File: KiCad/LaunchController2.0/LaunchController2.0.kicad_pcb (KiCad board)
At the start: 4 copper layers, 150 x 100 mm, 181 parts, among them J1 CONN_ICSP, J10 CONN_PANEL_BAORD_2, J11 CONN_AUDIO, J12 CONN_SPEAKER, J13 CONN_RS485, J2 CONN_USB, J3 USB_C_Receptacle_USB2.0_16P, J4 TO_CONVERTER, J5 FROM_CONVERTER, J6 DC_IN, J7 CONN_STATUS_PANEL, J8 CONN_BOARD_3, J9 CONN_PANEL_BAORD_1, Q1 TJ8S06M3L, Q2 2SC3325-Y, Q3 TJ8S06M3L, SW1 SW_Push, SW10 SW_Push, SW11 SW_Push, SW12 SW_Push, SW13 SW_Push, SW14 SW_Push, SW15 SW_Push, SW16 SW_Push, SW17 SW_Push, SW2 SW_Push, SW3 SW_Push, SW4 SW_Push, SW5 SW_Push, SW6 SW_Push, SW7 SW_Push, SW8 SW_Push, SW9 SW_Push, U1 ATmega2560-16A, U10 ADM2582E, U11 24LC256, U2 FT232RNL, U3 USBLC6-2SC6, U4 TPS2116DRL, U5 NJM7805SDL1, U6 INA219BIDCNT, U7 INA219BIDCNT, U9 DFPlayer, Y1 HUSG-16.000-20

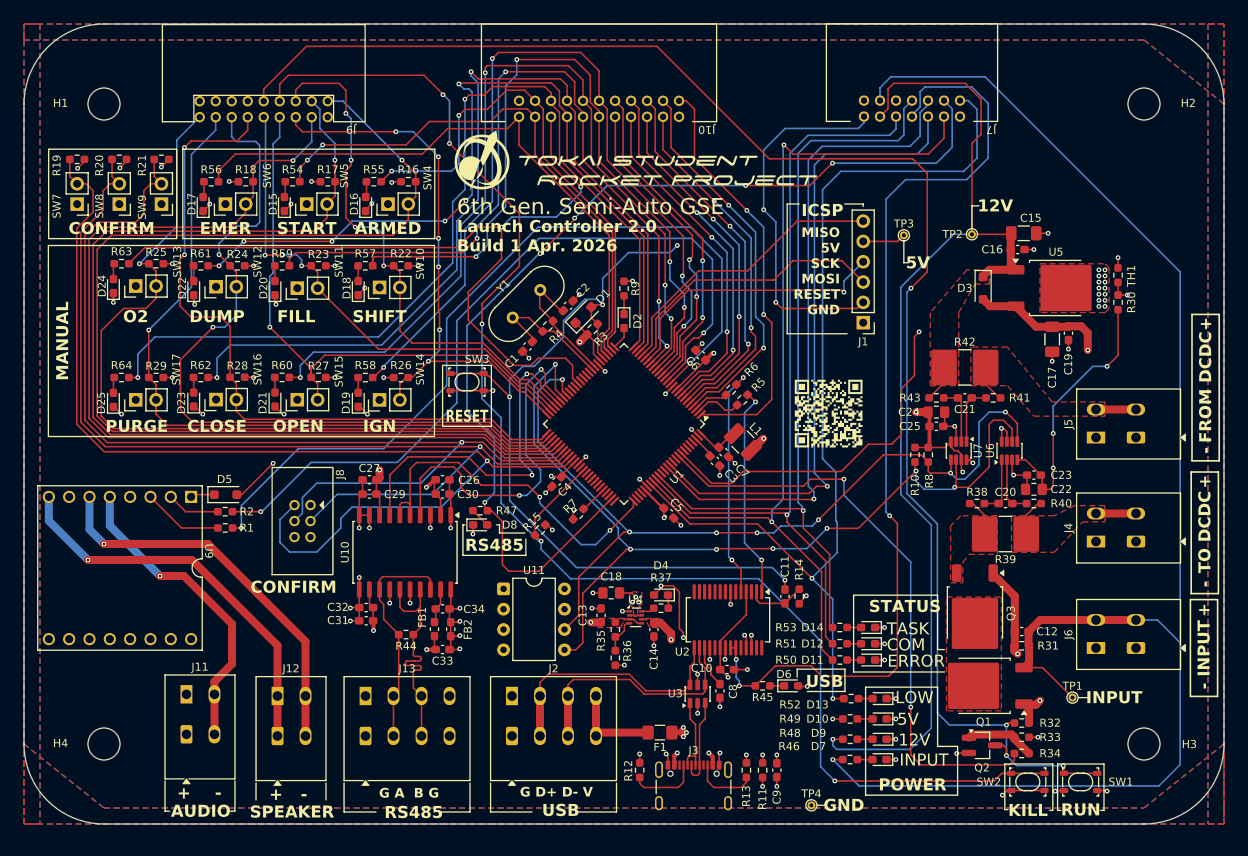
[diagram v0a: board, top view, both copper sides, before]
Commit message: 4層基板から2層基板へ仕様変更
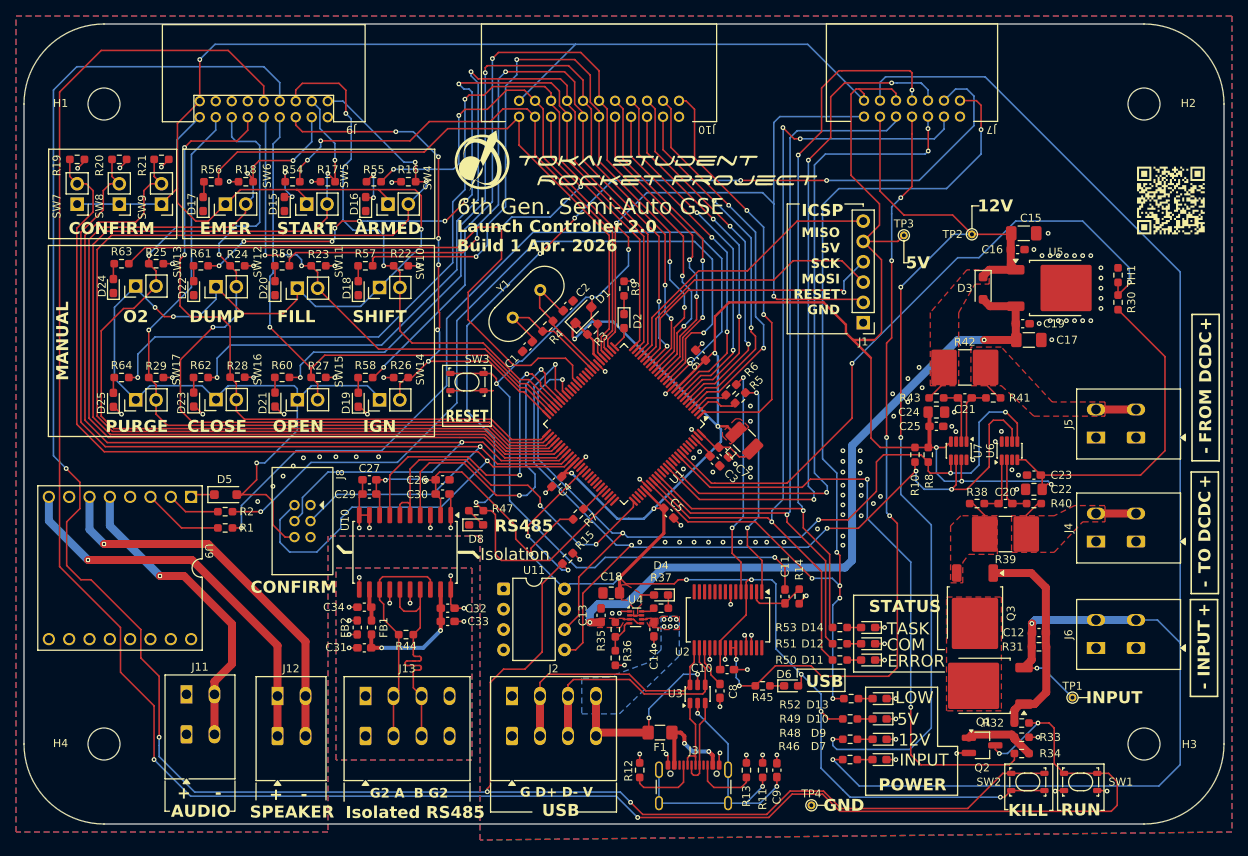
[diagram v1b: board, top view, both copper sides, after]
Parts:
- C33: value 0.01uF -> 0.1uF
- moved G*** 50.4 mm to (219.4, 73.1)
- moved FB2 11.7 mm to (117.7, 126.4)
- moved C32 10.2 mm to (129.0, 124.0), turned to 180 degrees
- moved C34 9.78 mm to (118.5, 123.9), turned to 0 degrees
- moved FB1 7.88 mm to (119.4, 126.4)
- moved C19 5.84 mm to (200.8, 88.5), turned to 180 degrees
- moved R15 4.94 mm to (143.9, 117.8)
- moved C33 3.57 mm to (129.0, 125.7)
- moved C31 3.39 mm to (118.5, 129.0)
- moved C17 2.92 mm to (201.6, 90.5), turned to 180 degrees
- moved R31 2.16 mm to (202.9, 128.9), turned to 0 degrees
- moved C12 2.16 mm to (202.9, 127.1), turned to 0 degrees
- moved D8 0.51 mm to (132.5, 113.6)
- moved R47 0.51 mm to (132.5, 111.8)
- moved R5 0.36 mm to (165.5, 97.7)
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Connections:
- U10 pad 12: /Peripheral/Visoin -> /Peripheral/Visoout
- U10 pad 19: /Peripheral/Visoout -> /Peripheral/Visoin
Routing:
- net CTL_KILL: track 186.2 -> 294.1 mm, vias 5 -> 6
- net CTL_RUN: track 192.7 -> 272.7 mm
- net VIN_5V: track 131.5 -> 89.6 mm
- net GND: track 132.1 -> 92.1 mm, vias 98 -> 144
- net CONN_LED_USB_ACCESS: track 121.4 -> 98.3 mm, vias 3 -> 6
- net CONN_LED_5V: track 699.5 -> 721.8 mm, vias 23 -> 22
- net CONN_LED_12V: track 136.8 -> 126.1 mm, vias 1 -> 3
- net USB_VBUS: track 35.2 -> 24.6 mm, vias 2 -> 8
- net GND2: track 23.8 -> 15.6 mm, vias 9 -> 10
- net CONN_LED_RS485_ACCESS: track 127.0 -> 133.4 mm
- net CONN_LED_TASK: track 99.8 -> 106.1 mm, vias 1 -> 3
- net Net-(F1-Pad1): track 17.3 -> 12.2 mm, vias 5 -> 2
- net CTL_RESET: track 162.1 -> 167.1 mm
- net 7SEG_DIO: track 82.7 -> 86.9 mm, vias 1 -> 3
- net VREF_THERMISTOR: track 79.2 -> 83.1 mm
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- added copper zone on B.Cu, net GND2
- added copper zone on F.Cu, net GND2
- added copper zone on B.Cu, net USB_VBUS
- removed copper zone on In1.Cu, net GND
- removed copper zone on In1.Cu, net GND2
- removed copper zone on In2.Cu, net Net-(F1-Pad1)
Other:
- copper layers 4 -> 2
- board text added: "G2 A B G2"
- board text added: "Isolated RS485"
- board text added: "Isolation"
- board text removed: "G A B G"

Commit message: Build-1いったん完成
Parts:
- added G***: LOGO, LOGO, F.Cu at (177.0, 99.8)
- added G***: LOGO, LOGO, F.Cu at (85.2, 119.0)
- J10: value CONN_PANEL_BAORD_2 -> CONN_PANEL_BOARD_2
- J9: value CONN_PANEL_BAORD_1 -> CONN_PANEL_BOARD_1
- moved G*** 53.6 mm to (166.3, 80.8)
- moved G*** 0.25 mm to (152.5, 68.4)
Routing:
- net GND: track 92.1 -> 216.2 mm, vias 144 -> 663
- net CONN_LED_5V: track 721.8 -> 729.2 mm
- net GND2: track 15.6 -> 21.1 mm, vias 10 -> 40
- net Net-(J13-Pin_3): track 29.4 -> 25.0 mm
- net UART0_TX: track 29.1 -> 31.2 mm
- net UART0_RX: track 27.7 -> 29.4 mm
- net CONN_LED_LOW_VOLTAGE: track 124.8 -> 126.3 mm, vias 6 -> 5
- net CTL_RUN: track 272.7 -> 273.9 mm
- net CTL_KILL: track 294.1 -> 295.0 mm
- net CONN_LED_SAFTEY: track 63.9 -> 64.7 mm
- net CONN_LED_INPUT: track 192.4 -> 191.7 mm
- net UART1_TX: track 41.9 -> 42.4 mm
- net CONN_LED_IGNITOR: track 105.0 -> 104.4 mm
- net Net-(J13-Pin_2): track 28.7 -> 29.2 mm
- net CTL_DUMP: track 95.8 -> 96.4 mm
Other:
- board text added: "1"
- board text added: "13"
- board text added: "14"
- board text added: "17"
- board text added: "18"
- board text added: "2"
- board text added: "21"
- board text added: "22"
- board text added: "4xΦ4"
- board text added: "DF51A-14DP-2DS"
- board text added: "DF51A-18DP-2DS"
- board text added: "DF51A-22DP-2DS"
- board text added: "DFPlayer Mini"
- board text added: "Document"
- board text added: "Launch Controller 2.0 Build-1 Apr. 2026"
- board text added: "PANEL"
- board text added: "STATUS PANEL"
- board text removed: "Launch Controller 2.0 Build 1 Apr. 2026"

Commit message: Build-1発行＆発注
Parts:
- removed R7: 10kR, Resistor_SMD:R_0603_1608Metric_Pad0.98x0.95mm_HandSolder
- turned D6 to 180 degrees
- turned D8 to 180 degrees
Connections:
- U1 pad 71: SPI_~{CS}_FeRAM0 -> unconnected-(U1-PA7-Pad71)
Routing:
- net USB_VBUS: track 24.6 -> 41.5 mm, vias 8 -> 3
- net CONN_LED_5V: track 729.2 -> 723.3 mm
- net TO_CONVERTER: track 9.82 -> 14.0 mm
- net +VSW: track 4.82 -> 8.50 mm
- net SPI_~{CS}_FeRAM0: track 3.46 -> 0.00 mm
- net Net-(D6-K): track 1.77 -> 4.21 mm
- net Net-(D8-A): track 2.52 -> 1.80 mm
- net 7SEG_DIO: track 86.9 -> 86.4 mm
- removed copper zone on B.Cu, net USB_VBUS
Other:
- board text added: "USB POWER"
- board text removed: "SPEAKER"

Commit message: USB＋，USB－の配線を修正
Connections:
- U3 pad 4: USB_D- -> USB_D+
- U3 pad 6: USB_D+ -> USB_D-
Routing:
- net USB_D-: track 30.4 -> 30.3 mm, vias 0 -> 2
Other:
- board text added: "Launch Controller 2.0 Build-2 May. 2026"
- board text removed: "Launch Controller 2.0 Build-1 Apr. 2026"
